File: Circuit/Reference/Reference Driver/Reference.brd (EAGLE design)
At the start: 160 x 100 mm, 12 parts

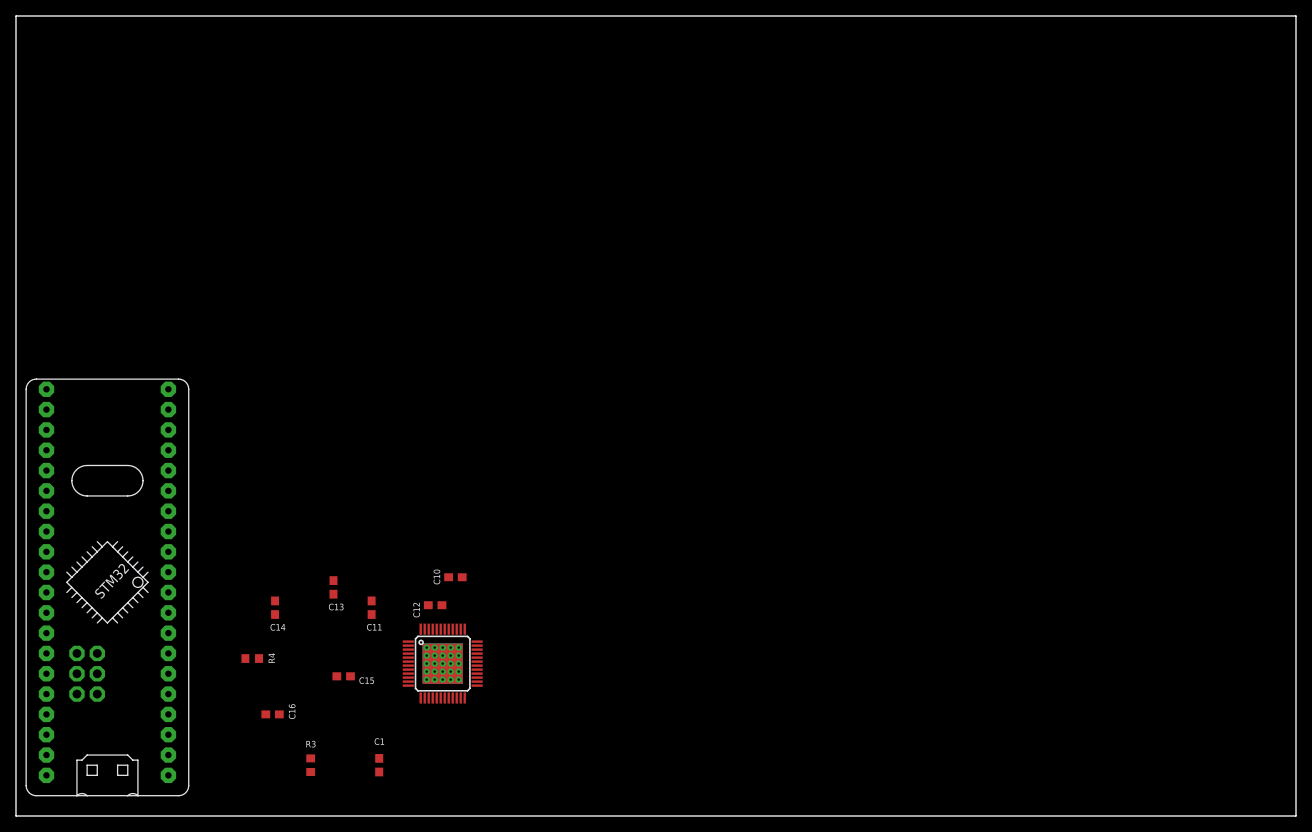
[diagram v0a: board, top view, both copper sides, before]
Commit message: Add the mosfets and their driver to the BLDC Driver sch
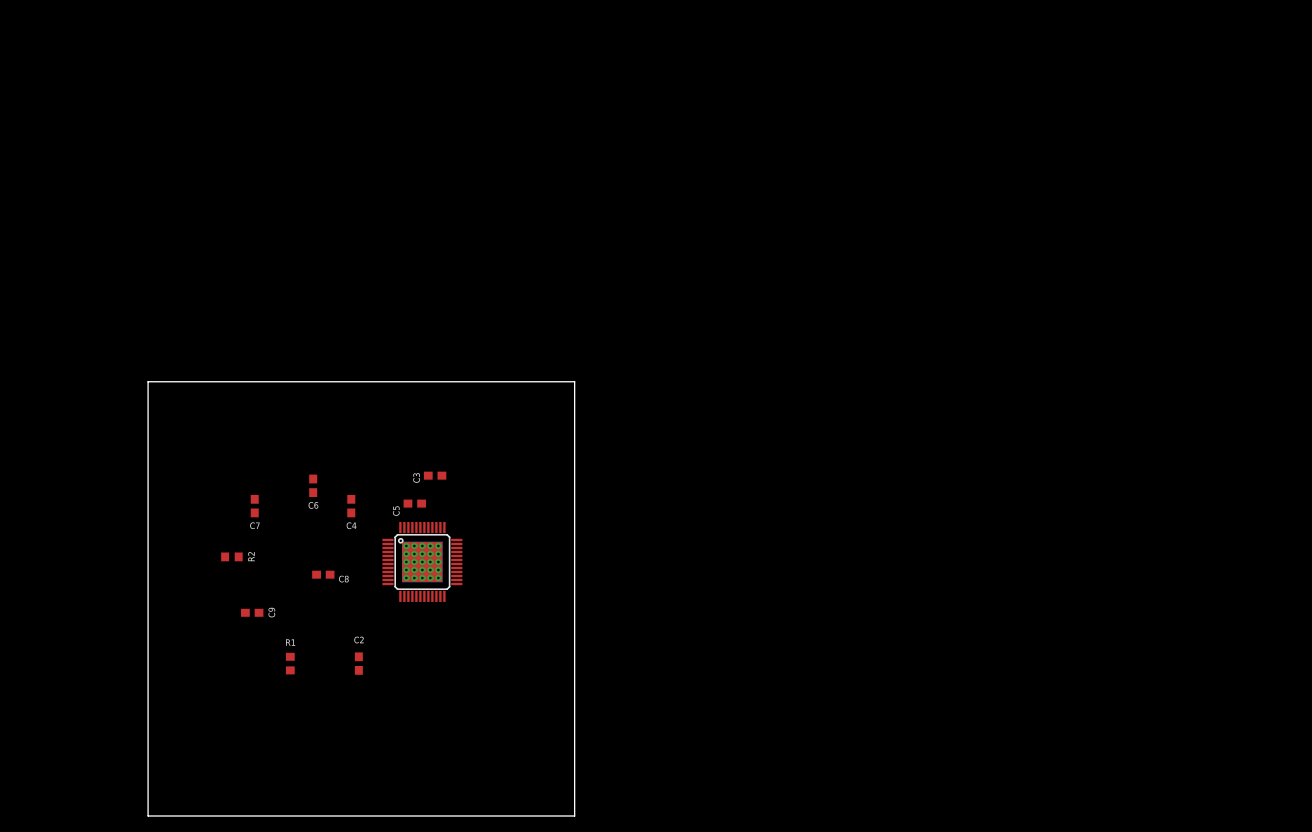
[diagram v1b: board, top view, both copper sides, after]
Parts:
- removed C1, C10, C15, C16: 1uF, rcl:C0603
- removed C11: 2.2uF, rcl:C0603
- removed C12: 4.7uF, rcl:C0603
- removed C13, C14: 47nF, rcl:C0603
- removed R3: 10k, rcl:R0603
- removed R4: 100, rcl:R0603
- removed U$3: DRV8305, BLDC project:PFB_S-PQFP-G48
- added C2, C3, C8, C9: 1uF, rcl:C0603
- added C4: 2.2uF, rcl:C0603
- added C5: 4.7uF, rcl:C0603
- added C6, C7: 47nF, rcl:C0603
- added R1: 10k, rcl:R0603
- added R2: 100, rcl:R0603
- U$1: value (none) -> DRV8305; device BluePill:BLUE_PILL_ADV -> BLDC project:PFB_S-PQFP-G48
- moved U$1 42.1 mm to (50.8, 31.8)
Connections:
- removed net A3: U$3.16
- removed net A4: U$3.17
- removed net A5: U$3.18
- removed net D1: U$3.1
- removed net D14: U$3.4
- removed net D15: U$3.6
- removed net D16: R3.2, U$3.13
- removed net D17: U$3.9
- removed net D18: U$3.10
- removed net D19: U$3.11
- removed net D20: U$3.12
- removed net D8: U$3.2
- removed net D9: U$3.8
- removed net GH_A1: U$3.36
- removed net GH_B1: U$3.29
- removed net GH_C1: U$3.28
- removed net GL_A1: U$3.33
- removed net GL_B1: U$3.32
- removed net GL_C1: U$3.25
- removed net N$15: C1.1, U$3.15
- removed net N$16: C10.1, U$3.37
- removed net N$17: C11.2, U$3.38
- removed net N$18: C13.2, U$3.40
- removed net N$19: C13.1, U$3.39
- removed net N$21: C14.2, U$3.43
- removed net N$22: C14.1, U$3.42
- removed net N$23: R4.1, U$3.44
- removed net N$24: C15.1, U$3.46
- removed net N$25: U$3.3
- removed net N$26: U$3.5
- removed net N$27: U$3.7
- removed net N$40: U$1.P$20
- removed net PA0: U$1.P$36
- removed net PA1: U$1.P$35
- removed net PA10: U$1.P$7
- removed net PA11: U$1.P$8
- removed net PA12: U$1.P$9
- removed net PA15: U$1.P$10
- removed net PA2: U$1.P$34
- removed net PA3: U$1.P$33
- removed net PA4: U$1.P$32
- removed net PA5: U$1.P$31
- removed net PA6: U$1.P$30
- removed net PA7: U$1.P$29
- removed net PA8: U$1.P$5
- removed net PA9: U$1.P$6
- removed net PB0: U$1.P$28
- removed net PB1: U$1.P$27
- removed net PB10: U$1.P$26
- removed net PB11: U$1.P$25
- removed net PB12: U$1.P$1
- removed net PB13: U$1.P$2
- removed net PB14: U$1.P$3
- removed net PB15: U$1.P$4
- removed net PB3: U$1.P$11
- removed net PB4: U$1.P$12
- removed net PB5: U$1.P$13
- removed net PB6: U$1.P$14
- removed net PB7: U$1.P$15
- removed net PB8: U$1.P$16
- removed net PB9: U$1.P$17
- removed net PC13: U$1.P$39
- removed net PC14: U$1.P$38
- removed net PC15: U$1.P$37
- removed net SH_A1: U$3.35
- removed net SH_B1: U$3.30
- removed net SH_C1: U$3.27
- removed net SL_A1: U$3.23, U$3.34
- removed net SL_B1: U$3.21, U$3.31
- removed net SL_C1: U$3.19, U$3.26
- removed net VIN: U$1.P$40
- new net A0: U$1.16
- new net A1: U$1.17
- new net A2: U$1.18
- new net D10: U$1.9
- new net D11: U$1.10
- new net D12: U$1.11
- new net D13: U$1.12
- new net D2: U$1.1
- new net D3: U$1.2
- new net D4: U$1.8
- new net D5: U$1.4
- new net D6: U$1.6
- new net D7: R1.2, U$1.13
- new net GH_A: U$1.36
- new net GH_B: U$1.29
- new net GH_C: U$1.28
- new net GL_A: U$1.33
- new net GL_B: U$1.32
- new net GL_C: U$1.25
- new net N$1: C2.1, U$1.15
- new net N$10: U$1.3
- new net N$11: U$1.5
- new net N$12: U$1.7
- new net N$2: C3.1, U$1.37
- new net N$5: C6.1, U$1.39
- new net N$6: C7.2, U$1.43
- new net N$7: C7.1, U$1.42
- new net N$8: R2.1, U$1.44
- new net N$9: C8.1, U$1.46
- new net SH_A: U$1.35
- new net SH_B: U$1.30
- new net SH_C: U$1.27
- new net SL_A: U$1.23, U$1.34
- new net SL_B: U$1.21, U$1.31
- new net SL_C: U$1.19, U$1.26
- net +5V: now also C9.1, R1.1, U$1.48; no longer C16.1, R3.1, U$3.48
- net GND: now also C2.2, C3.2, C5.2, C8.2, C9.2, U$1.14, U$1.20, U$1.22, U$1.24, U$1.45, U$1.P$1, U$1.P$10, U$1.P$11, U$1.P$12, U$1.P$13, U$1.P$14, U$1.P$15, U$1.P$16, U$1.P$17, U$1.P$18, U$1.P$2, U$1.P$20, U$1.P$23, U$1.P$24, U$1.P$25, U$1.P$26, U$1.P$27, U$1.P$3, U$1.P$4, U$1.P$5, U$1.P$6, U$1.P$7, U$1.P$8, U$1.P$9; no longer C1.2, C10.2, C12.2, C15.2, C16.2, U$3.14, U$3.20, U$3.22, U$3.24, U$3.45, U$3.P$1, U$3.P$10, U$3.P$11, U$3.P$12, U$3.P$13, U$3.P$14, U$3.P$15, U$3.P$16, U$3.P$17, U$3.P$18, U$3.P$19, U$3.P$2, U$3.P$20, U$3.P$21, U$3.P$22, U$3.P$23, U$3.P$24, U$3.P$25, U$3.P$26, U$3.P$27, U$3.P$3, U$3.P$4, U$3.P$5, U$3.P$6, U$3.P$7, U$3.P$8, U$3.P$9
- net N$3: now also C4.2, U$1.38; no longer U$1.P$23
- net N$4: now also C6.2, U$1.40; no longer U$1.P$24
- net VCC: now also C4.1, C5.1, R2.2, U$1.41; no longer C11.1, C12.1, R4.2, U$1.P$18, U$3.41
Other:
- board size 160 x 100 mm -> 53.3 x 54.3 mm
